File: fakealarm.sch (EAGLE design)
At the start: 17 parts, among them IC1 NE555N, Q1 2N3904, X1 RUN, X2 BAT, X3 GND, X4 +, X5 LED

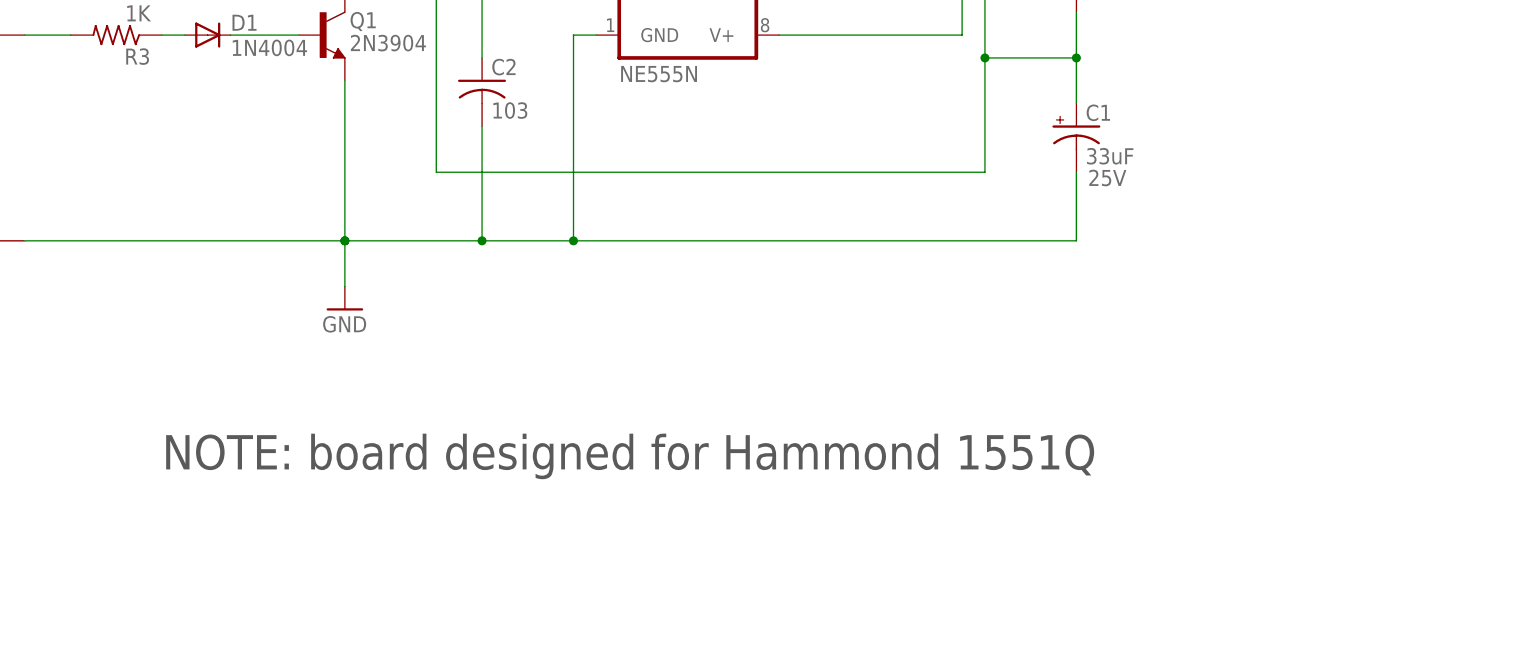
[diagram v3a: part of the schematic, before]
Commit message: redesigned for hammond 1551P (taller enclosure), respec'ed 33uF cap height and voltage, added documentation for max board height' '
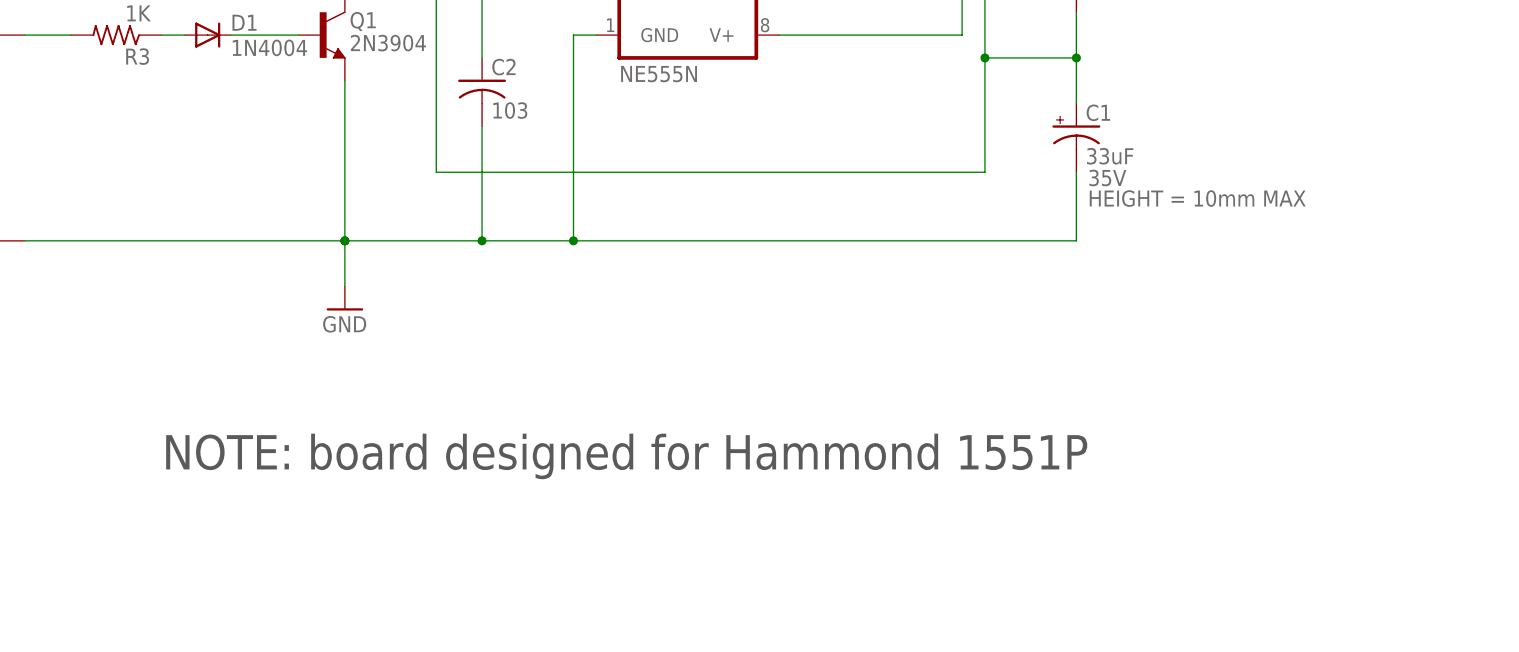
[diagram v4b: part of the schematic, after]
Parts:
- C1: HEIGHT (none) -> 10mm MAX; VOLTAGE 25V -> 35V
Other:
- note added: "NOTE: board designed for Hammond 1551P"
- note removed: "NOTE: board designed for Hammond 1551Q"
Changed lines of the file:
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@@
 <part name="R5" library="rcl" deviceset="R-US_" device="0207/10" value="1K"/>
 <part name="C1" library="rcl" deviceset="CPOL-US" device="E2.5-6" value="33uF">
-<attribute name="VOLTAGE" value="25V"/>
+<attribute name="HEIGHT" value="10mm MAX"/>
+<attribute name="VOLTAGE" value="35V"/>
 </part>
 <part name="SUPPLY1" library="SparkFun-Aesthetics" deviceset="12V" device=""/>
@@
 <text x="154.94" y="22.86" size="3.81" layer="94">FAKE ALARM BLINKER</text>
 <text x="231.14" y="22.86" size="3.81" layer="94">R0.1</text>
-<text x="88.9" y="48.26" size="3.81" layer="97">NOTE: board designed for Hammond 1551Q</text>
+<text x="88.9" y="48.26" size="3.81" layer="97">NOTE: board designed for Hammond 1551P</text>
 </plain>
 <instances>
@@
 <instance part="C1" gate="G$1" x="190.5" y="86.36">
 <attribute name="VOLTAGE" x="191.77" y="79.756" size="1.778" layer="96"/>
+<attribute name="HEIGHT" x="191.77" y="77.47" size="1.778" layer="96" display="both"/>
 </instance>
 <instance part="SUPPLY1" gate="G$1" x="109.22" y="144.78"/>

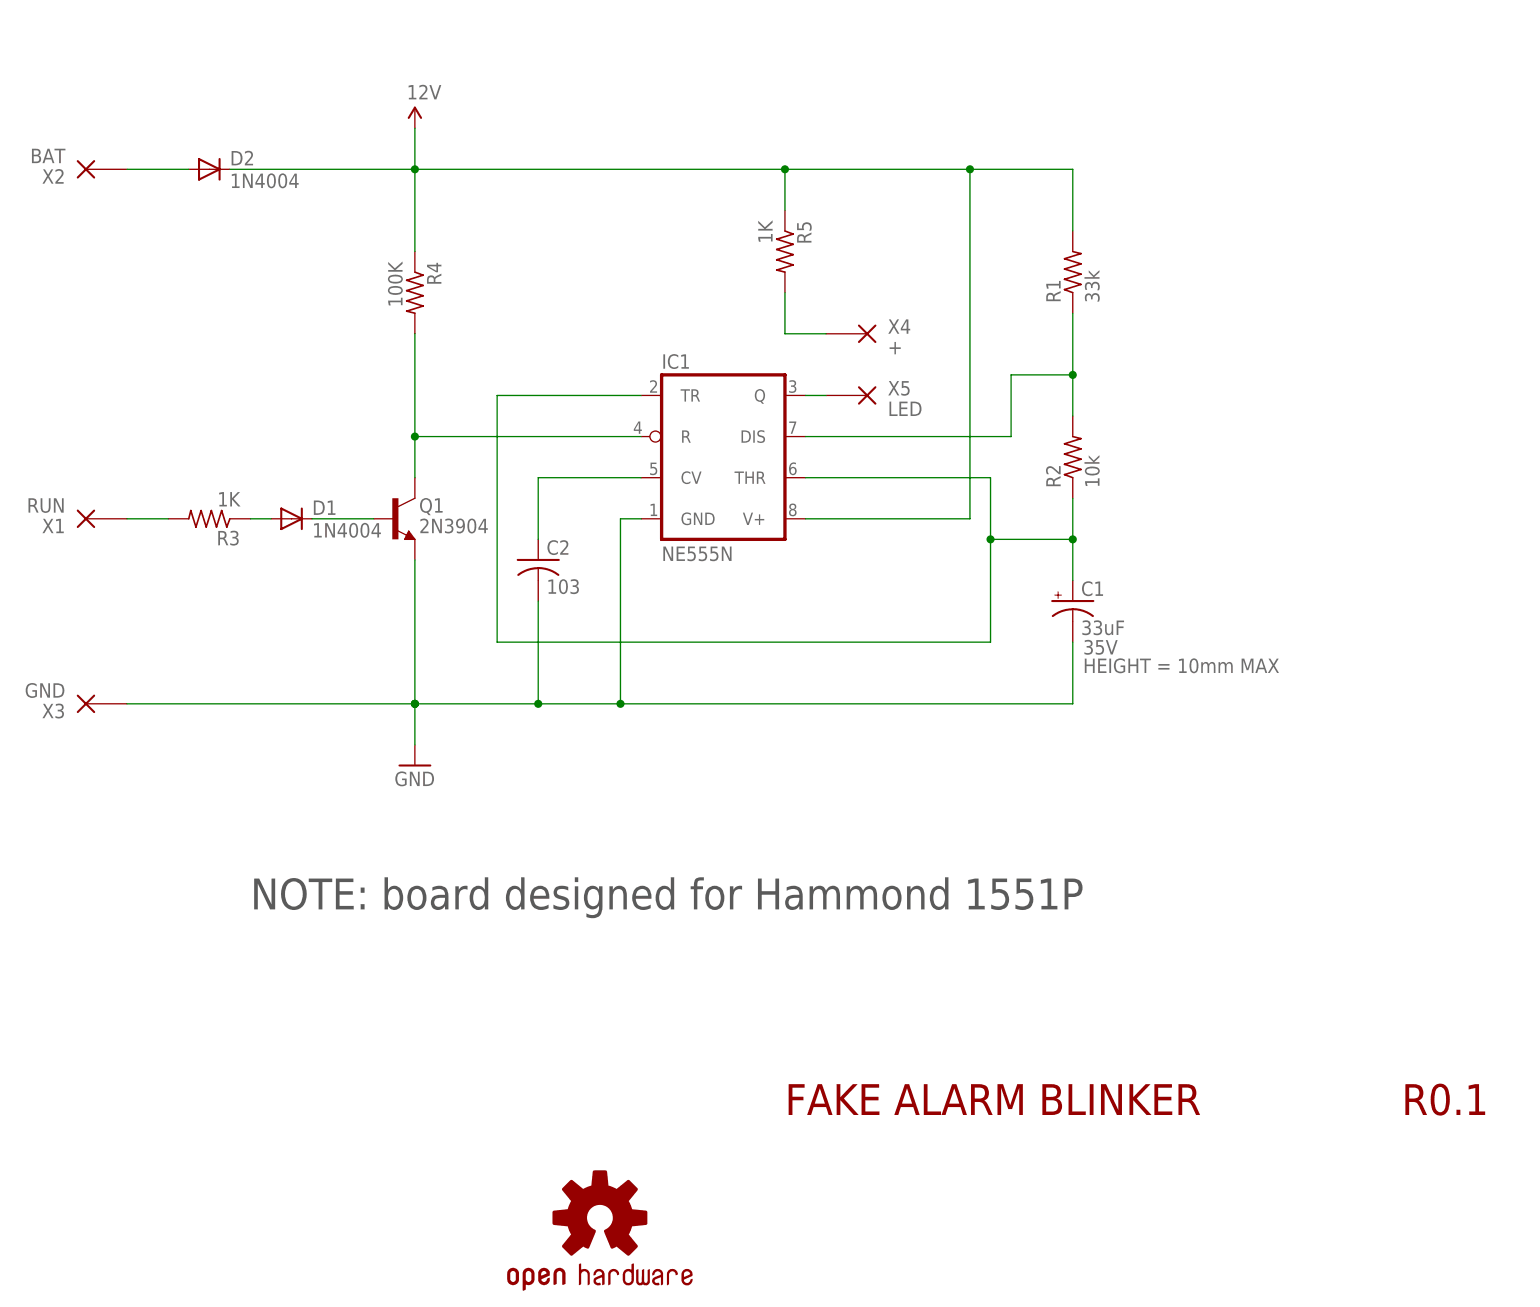
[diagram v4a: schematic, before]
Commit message: replaced NPN with N-channel MOSFET tied to power, replaced 100k rst with 10k
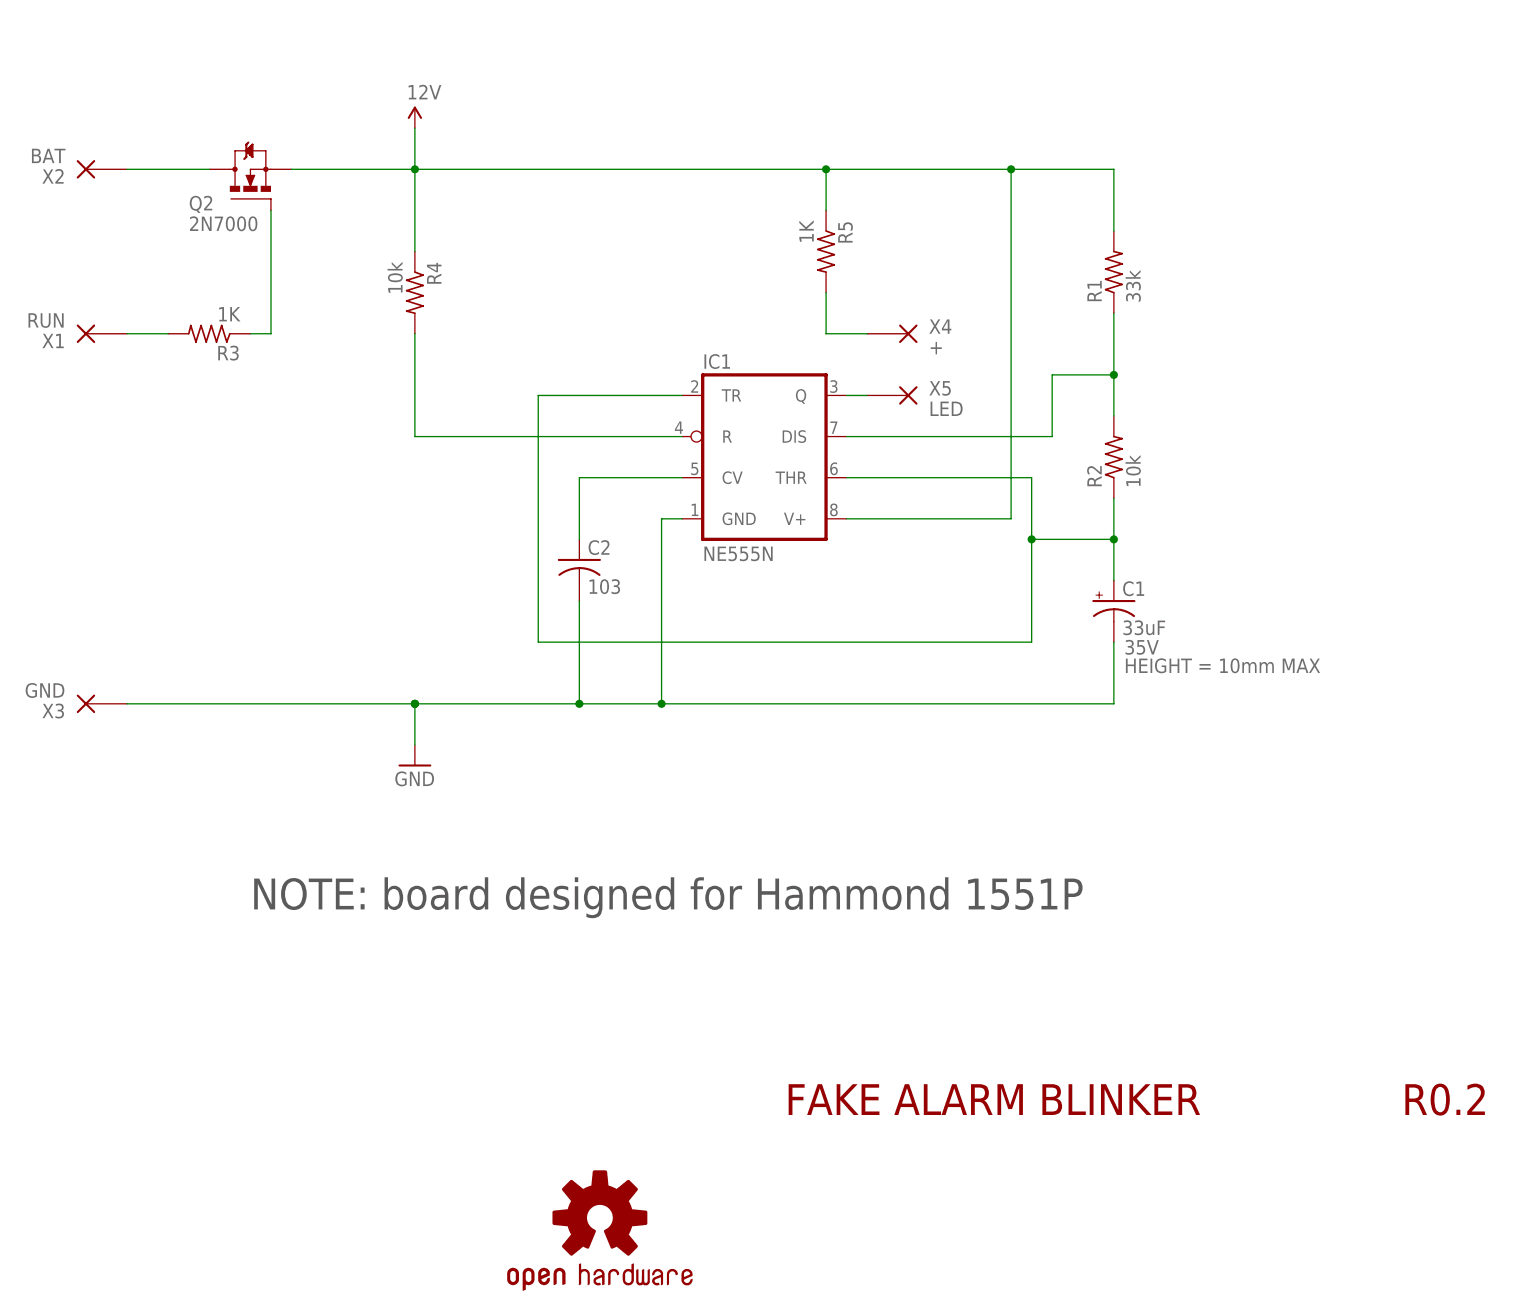
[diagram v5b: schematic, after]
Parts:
- removed D1, D2: 1N4004, diode:1N4004
- removed Q1: 2N3904, bt_transistor:2N3904TO92
- added Q2: 2N7000, ads4:MOSFET-NTO92
- R4: value 100K -> 10k
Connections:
- removed net N$2: D1.C, Q1.B
- net 12V: now also Q2.S; no longer D2.C
- net GND: no longer Q1.E
- net N$1: now also Q2.G; no longer D1.A
- net N$11: no longer Q1.C
- net N$6: now also Q2.D; no longer D2.A
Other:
- note added: "R0.2"
- note removed: "R0.1"
- moved on the sheet: C1, C2, IC1, R1, R2, R3, R5, X1, X4, X5

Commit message: Revised switch to use two mosfets to switch entire 555, revised layout, silk, added enclosure info to board
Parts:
- added Q1: 2N7000, ads4:MOSFET-NTO92
- IC1: value NE555N -> LTC555
- LOGO1: value OSHW-LOGOS -> OSHW-LOGOM; device SparkFun-Aesthetics:OSHW-LOGOS -> SparkFun-Aesthetics:OSHW-LOGOM
- R3: value 1K -> 10k
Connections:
- removed net N$11: IC1.R, R4.2
- removed net N$6: Q2.D, X2.P
- new net N$2: Q1.G, R3.1, X1.P
- net 12V: now also IC1.R, X2.P; no longer Q2.S
- net GND: now also Q1.S, Q2.S, R3.2; no longer IC1.GND
- net N$1: now also Q1.D, R4.2; no longer R3.1
- net N$5: now also IC1.GND, Q2.D; no longer R3.2, X1.P
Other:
- moved on the sheet: C1, C2, IC1, Q2, R1, R2, R3, R4, R5, X1, X2, X3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
